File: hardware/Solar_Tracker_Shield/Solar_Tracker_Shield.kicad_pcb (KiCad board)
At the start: 2 copper layers, 70.3 x 53.3 mm, 13 parts, among them J1 TO LDR BOARD, J2 SERVO, J3 SERVO, J4 TO SOLAR SHIELD, U5 ARDUINO-101-SHIELD

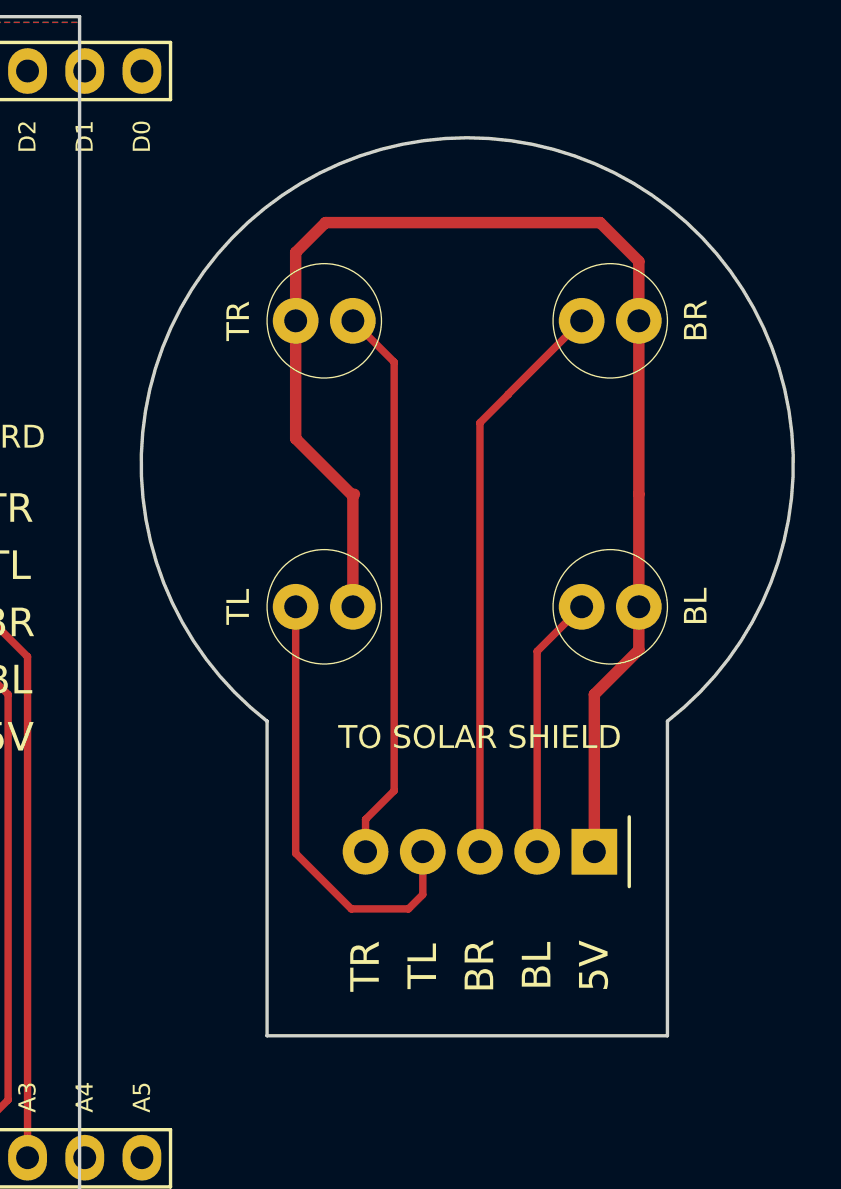
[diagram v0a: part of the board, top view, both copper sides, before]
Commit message: Split new LDR and old Solar Tracker boards.
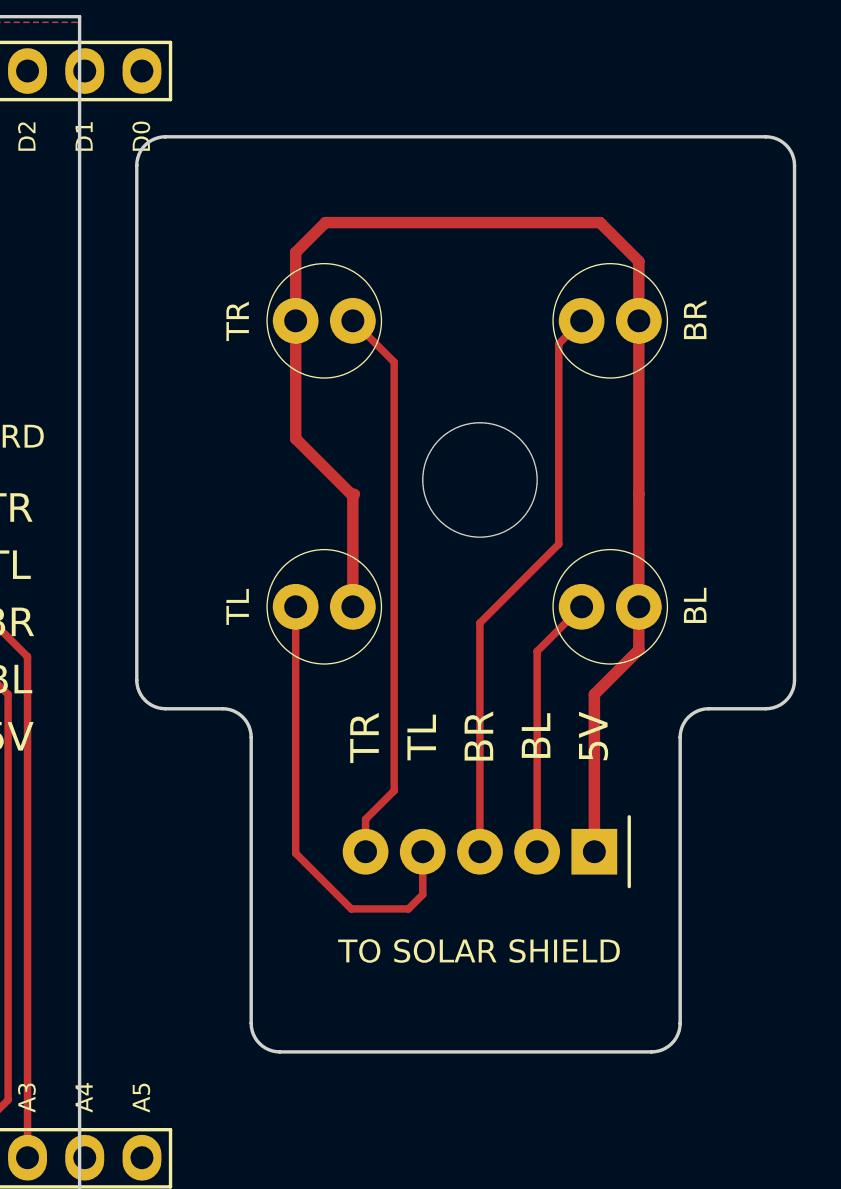
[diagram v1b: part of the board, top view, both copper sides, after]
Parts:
- added V: HOLE-PLATED-200MIL, Wickerlib:HOLE-UNPLATED-200MIL, F.Cu at (189.5, 93.7)
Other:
- board size 70.3 x 53.3 mm -> 70.4 x 53.3 mm
- board text added: "LDR Board v1.1"
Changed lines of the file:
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@@
-(kicad_pcb (version 4) (host pcbnew 4.0.3+e1-6302~38~ubuntu14.04.1-stable)
+(kicad_pcb (version 4) (host pcbnew 4.0.5-e0-6337~49~ubuntu16.04.1)
   (general
     (links 31)
     (no_connects 1)
-    (area 104.572999 69.031 203.47521 129.272)
+    (area 104.572999 69.031 203.529001 129.272)
     (thickness 1.6)
-    (drawings 55)
+    (drawings 63)
     (tracks 74)
     (zones 0)
-    (modules 13)
+    (modules 14)
     (nets 13)
   )
@@
   )
   (setup
-    (last_trace_width 0.254)
+    (last_trace_width 0.3302)
     (user_trace_width 0.1524)
     (user_trace_width 0.254)
@@
     )
     (fp_circle (center 0 0) (end 0 0.254) (layer F.Fab) (width 0.2))
-    (fp_text user "TO SOLAR SHIELD" (at -5.08 5.08 360) (layer F.SilkS)
+    (fp_text user "TO SOLAR SHIELD" (at 4.445 5.08 540) (layer F.SilkS)
       (effects (font (size 1.016 1.016) (thickness 0.2032)))
     )
@@
       (net 6 /A3/TOPRIGHT))
   )
+  (module Wickerlib:HOLE-UNPLATED-200MIL (layer F.Cu)
+    (at 189.484 93.726)
+    (descr "Standard 2x20 DIP header based on KiCad Pin Header 2x20")
+    (tags "pin header")
+    (fp_text reference V (at 0 -2) (layer F.SilkS) hide
+      (effects (font (size 1.016 1.016) (thickness 0.1524)))
+    )
+    (fp_text value HOLE-PLATED-200MIL (at -2.1 2.88 90) (layer F.Fab) hide
+      (effects (font (size 1 1) (thickness 0.15)))
+    )
+    (pad "" np_thru_hole circle (at 0 0) (size 5.08 5.08) (drill 5.08) (layers *.Cu))
+  )
+  (gr_arc (start 180.594 117.856) (end 180.594 119.126) (angle 90) (layer Edge.Cuts) (width 0.15))
+  (gr_arc (start 199.644 105.156) (end 198.374 105.156) (angle 90) (layer Edge.Cuts) (width 0.15))
+  (gr_arc (start 178.054 105.156) (end 178.054 103.886) (angle 90) (layer Edge.Cuts) (width 0.15))
+  (gr_arc (start 197.104 117.856) (end 198.374 117.856) (angle 90) (layer Edge.Cuts) (width 0.15))
+  (gr_arc (start 202.184 102.616) (end 203.454 102.616) (angle 90) (layer Edge.Cuts) (width 0.15))
+  (gr_arc (start 175.514 102.616) (end 175.514 103.886) (angle 90) (layer Edge.Cuts) (width 0.15))
+  (gr_arc (start 175.514 79.756) (end 174.244 79.756) (angle 90) (layer Edge.Cuts) (width 0.15))
+  (gr_arc (start 202.184 79.756) (end 202.184 78.486) (angle 90) (layer Edge.Cuts) (width 0.15))
+  (gr_line (start 202.184 103.886) (end 199.644 103.886) (layer Edge.Cuts) (width 0.15))
+  (gr_line (start 203.454 79.756) (end 203.454 102.616) (layer Edge.Cuts) (width 0.15))
+  (gr_line (start 175.514 103.886) (end 178.054 103.886) (layer Edge.Cuts) (width 0.15))
+  (gr_line (start 174.244 79.756) (end 174.244 102.616) (layer Edge.Cuts) (width 0.15))
+  (gr_line (start 202.184 78.486) (end 175.514 78.486) (layer Edge.Cuts) (width 0.15))
   (gr_text "Solar Shield v1.0" (at 161.544 70.231) (layer F.Fab)
     (effects (font (size 1.5 1.5) (thickness 0.3)))
   )
-  (gr_text "LDR Board v1.0" (at 188.849 75.946) (layer F.Fab)
+  (gr_text "LDR Board v1.1" (at 188.849 75.946) (layer F.Fab)
     (effects (font (size 1.5 1.5) (thickness 0.3)))
   )
-  (gr_line (start 197.739 118.409073) (end 197.739 104.439073) (layer F.Fab) (width 0.15))
-  (gr_line (start 179.959 118.409073) (end 197.739 118.409073) (layer F.Fab) (width 0.15))
-  (gr_line (start 180.029981 104.439073) (end 180.029981 118.409073) (layer F.Fab) (width 0.15))
-  (gr_arc (start 188.849 93.009073) (end 179.959 104.439073) (angle 284.2) (layer F.Fab) (width 0.15))
   (gr_line (start 171.704 126.746) (end 171.704 72.771) (layer F.Fab) (width 0.1524))
   (gr_line (start 132.969 126.746) (end 171.704 126.746) (layer F.Fab) (width 0.1524))
@@
     (effects (font (size 1.27 1.27) (thickness 0.254)))
   )
-  (gr_text 5V (at 194.564 115.316 90) (layer F.SilkS)
-    (effects (font (size 1.27 1.27) (thickness 0.254)))
-  )
-  (gr_text TR (at 184.404 115.316 90) (layer F.SilkS)
-    (effects (font (size 1.27 1.27) (thickness 0.254)))
-  )
-  (gr_text TL (at 186.944 115.316 90) (layer F.SilkS)
-    (effects (font (size 1.27 1.27) (thickness 0.254)))
-  )
-  (gr_text BR (at 189.484 115.316 90) (layer F.SilkS)
-    (effects (font (size 1.27 1.27) (thickness 0.254)))
-  )
-  (gr_text BL (at 192.024 115.316 90) (layer F.SilkS)
-    (effects (font (size 1.27 1.27) (thickness 0.254)))
-  )
-  (gr_line (start 197.809981 118.409073) (end 197.809981 104.439073) (layer Edge.Cuts) (width 0.15))
-  (gr_line (start 180.029981 118.409073) (end 197.809981 118.409073) (layer Edge.Cuts) (width 0.15))
-  (gr_line (start 180.029981 104.439073) (end 180.029981 118.409073) (layer Edge.Cuts) (width 0.15))
-  (gr_arc (start 188.919981 93.009073) (end 180.029981 104.439073) (angle 284.2500334) (layer Edge.Cuts) (width 0.15))
+  (gr_text 5V (at 194.564 105.156 90) (layer F.SilkS)
+    (effects (font (size 1.27 1.27) (thickness 0.254)))
+  )
+  (gr_text TR (at 184.404 105.156 90) (layer F.SilkS)
+    (effects (font (size 1.27 1.27) (thickness 0.254)))
+  )
+  (gr_text TL (at 186.944 105.156 90) (layer F.SilkS)
+    (effects (font (size 1.27 1.27) (thickness 0.254)))
+  )
+  (gr_text BR (at 189.484 105.156 90) (layer F.SilkS)
+    (effects (font (size 1.27 1.27) (thickness 0.254)))
+  )
+  (gr_text BL (at 192.024 105.156 90) (layer F.SilkS)
+    (effects (font (size 1.27 1.27) (thickness 0.254)))
+  )
+  (gr_line (start 198.374 117.856) (end 198.374 105.156) (layer Edge.Cuts) (width 0.15))
+  (gr_line (start 180.594 119.126) (end 197.104 119.126) (layer Edge.Cuts) (width 0.15))
+  (gr_line (start 179.324 105.156) (end 179.324 117.856) (layer Edge.Cuts) (width 0.15))
   (gr_text GND (at 135.509 110.236) (layer F.SilkS)
     (effects (font (size 1.27 1.27) (thickness 0.254)))
@@
   (segment (start 192.024 110.236) (end 192.024 101.335054) (width 0.3302) (layer F.Cu) (net 9))
   (segment (start 192.024 101.335054) (end 193.999981 99.359073) (width 0.3302) (layer F.Cu) (net 9))
-  (segment (start 189.484 91.186) (end 189.484 110.236) (width 0.3302) (layer F.Cu) (net 10))
-  (segment (start 190.743054 89.926946) (end 189.484 91.186) (width 0.3302) (layer F.Cu) (net 10))
-  (segment (start 190.743054 89.916) (end 190.743054 89.926946) (width 0.3302) (layer F.Cu) (net 10))
-  (segment (start 193.999981 86.659073) (end 190.743054 89.916) (width 0.3302) (layer F.Cu) (net 10))
+  (segment (start 192.983982 96.576018) (end 189.484 100.076) (width 0.3302) (layer F.Cu) (net 10))
+  (segment (start 189.484 100.076) (end 189.484 110.236) (width 0.3302) (layer F.Cu) (net 10))
+  (segment (start 193.999981 86.659073) (end 192.983982 87.675072) (width 0.3302) (layer F.Cu) (net 10))
+  (segment (start 192.983982 87.675072) (end 192.983982 96.576018) (width 0.3302) (layer F.Cu) (net 10))
   (segment (start 186.309 112.776) (end 186.944 112.141) (width 0.3302) (layer F.Cu) (net 11))
   (segment (start 186.944 112.141) (end 186.944 110.236) (width 0.3302) (layer F.Cu) (net 11))
